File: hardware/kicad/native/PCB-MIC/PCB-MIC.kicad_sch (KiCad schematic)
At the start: 4 parts, among them J1 5040500691

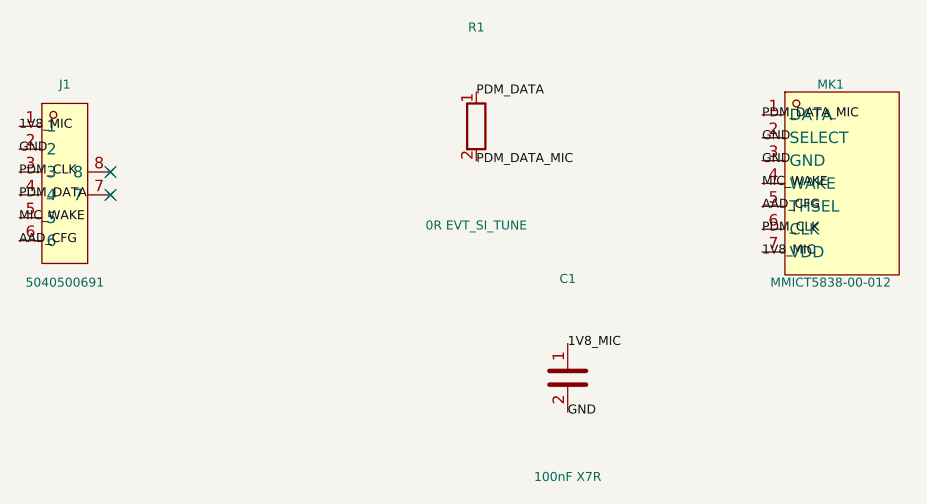
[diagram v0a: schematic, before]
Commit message: Fix PCB-MIC KiCad Altium connectivity parity
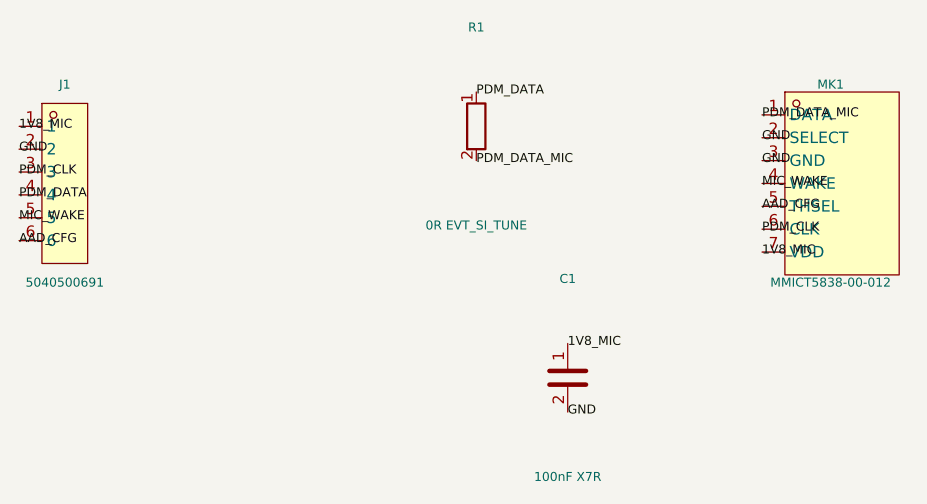
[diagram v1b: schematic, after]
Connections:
- no-connect marks 2 -> 0
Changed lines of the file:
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@@
     (comment 2 "NOT FOR MANUFACTURE until Review A/B")
   )
-  (no_connect (at 40.64 71.12))
-  (no_connect (at 40.64 68.58))
   (label "1V8_MIC" (at 30.48 63.5 0)
     (effects (font (size 1 1)))
@@
     (pin "5")
     (pin "6")
-    (pin "7")
-    (pin "8")
     (instances
       (project "PCB-MIC"
